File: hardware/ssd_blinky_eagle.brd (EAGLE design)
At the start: 48.3 x 25.4 mm, 13 parts, among them U1 Tiny85-20-SMT

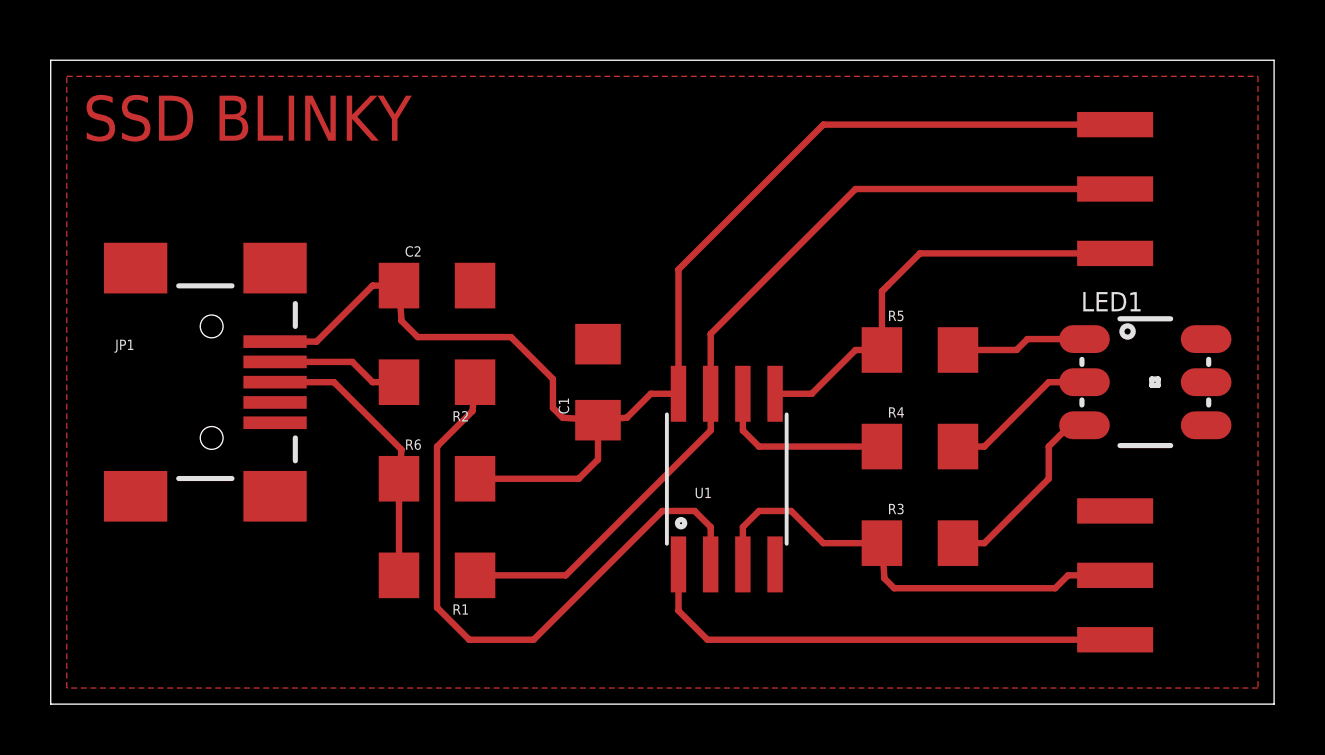
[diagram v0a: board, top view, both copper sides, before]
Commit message: complete candidate board layout in eagle
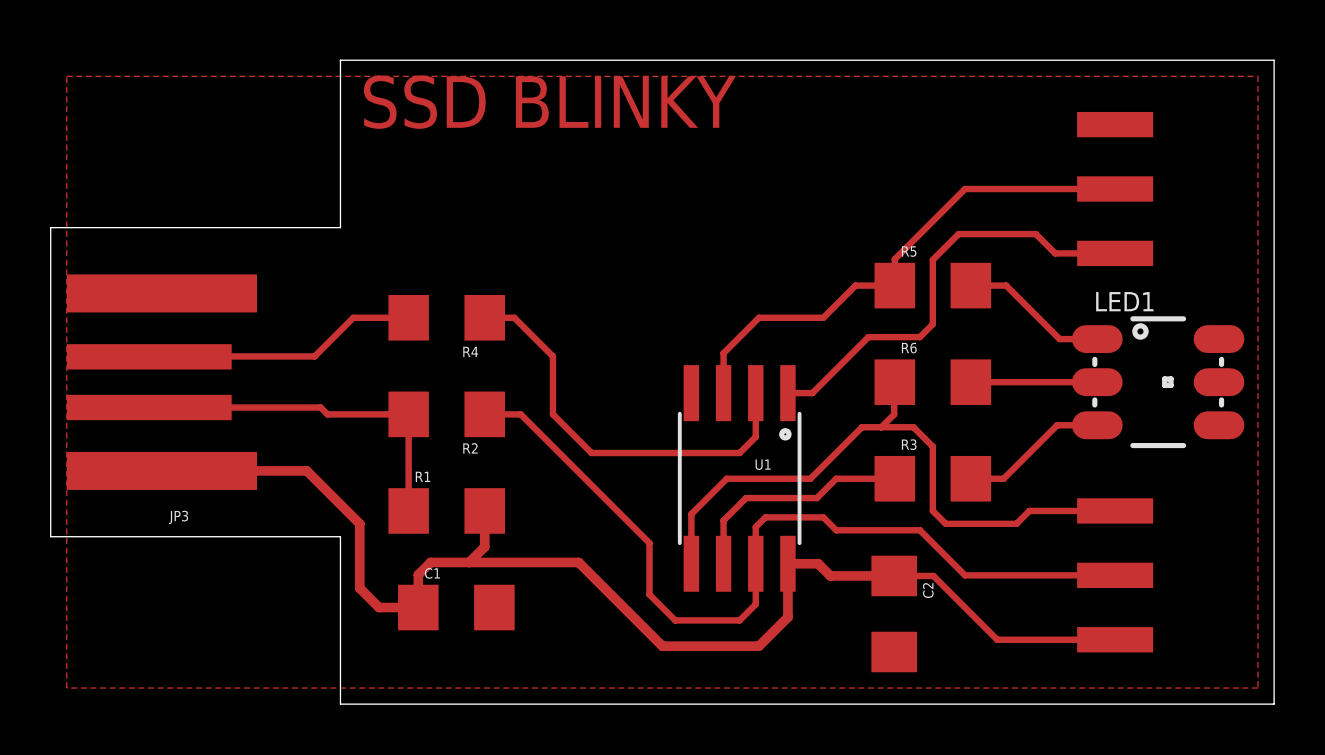
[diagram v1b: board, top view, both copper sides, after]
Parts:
- removed JP4: (no value), SparkFun-Connectors:1X03_SMD_RA_MALE
- added JP3: USBPCB, SparkFun-Connectors:USB-A-PCB
- JP1: value USBSMD -> (none); device SparkFun-Connectors:USB-MINIB -> SparkFun-Connectors:1X03_SMD_RA_MALE
- moved JP1 41.3 mm to (47.0, 5.08), turned to 90 degrees
- moved C2 22.2 mm to (33.3, 3.56), turned to 270 degrees
- moved R6 19.9 mm to (34.8, 12.7)
- moved R4 19.3 mm to (15.6, 15.2), turned to 180 degrees
- moved C1 10.5 mm to (16.0, 3.81), turned to 0 degrees
- moved R3 2.59 mm to (34.8, 8.89)
- moved R5 2.59 mm to (34.8, 16.5)
- moved R1 2.57 mm to (15.6, 7.62), turned to 0 degrees
- moved R2 1.33 mm to (15.6, 11.4)
- moved LED1 0.51 mm to (43.7, 12.7)
- moved U1 0.51 mm to (27.2, 8.89), turned to 180 degrees
- renumbered JP5 to JP2
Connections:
- net +5V: now also JP1.1, JP3.5V, R1.2; no longer JP1.VBUS, JP2.3, R6.2
- net D+: now also JP3.USB_P, R1.1, R2.2; no longer JP1.D+, R1.2, R6.1
- net D-: now also JP3.USB_M, R4.2; no longer JP1.D-, R2.2
- net GND: now also JP2.3, JP3.GND; no longer JP1.GND, JP4.3
- net MISO: now also JP2.2, R5.1; no longer JP4.2, R3.1
- net MOSI: now also JP1.3, R6.1; no longer JP2.1, R5.1
- net N$1: now also R4.1; no longer R2.1
- net N$2: now also R3.1; no longer R4.1
- net N$4: now also R6.2; no longer R4.2
- net RST: now also JP2.1; no longer JP4.1
- net SCK: now also JP1.2, R2.1; no longer JP2.2, R1.1
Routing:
- net N$1: track 24.6 -> 16.2 mm
- net MOSI: track 17.1 -> 25.4 mm
- net D-: track 5.22 -> 10.9 mm
- net D+: track 11.1 -> 14.2 mm
- net N$2: track 7.20 -> 9.14 mm
- net N$6: track 7.66 -> 5.86 mm
- net MISO: track 18.6 -> 20.3 mm
- net +5V: track 52.0 -> 50.3 mm
- net RST: track 19.5 -> 18.2 mm
- net N$4: track 6.04 -> 4.99 mm
- net N$5: track 5.17 -> 5.86 mm
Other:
- outline, holes or cut-outs redrawn
